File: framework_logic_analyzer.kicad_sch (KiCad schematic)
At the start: 76 parts, among them IC1 TXU0104QWBQARQ1, IC2 TXU0104QWBQARQ1, IC3 TXU0104QWBQARQ1, IC4 TXU0104QWBQARQ1, IC5 CYUSB3014-BZXC, J1 Conn_02x08_Odd_Even, J2 Conn_02x08_Odd_Even, J3 Conn_ARM_JTAG_SWD_10, Q1 MMBT3904, Q2 MMBT3904, Q3 MMBT3904, U5 M24M02-DR, Y1 19.200 MHz

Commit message: New header and enclosure
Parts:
- J1, J2: footprint Connector_PinSocket_1.27mm:PinSocket_2x08_P1.27mm_Horizontal -> 20021311-00016T4LF:20021311-00016T4LF
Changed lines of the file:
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@@
       (effects (font (size 1.27 1.27)))
     )
-    (property "Footprint" "Connector_PinSocket_1.27mm:PinSocket_2x08_P1.27mm_Horizontal" (at 350.52 149.86 0)
+    (property "Footprint" "20021311-00016T4LF:20021311-00016T4LF" (at 350.52 149.86 0)
       (effects (font (size 1.27 1.27)) hide)
     )
@@
       (effects (font (size 1.27 1.27)))
     )
-    (property "Footprint" "Connector_PinSocket_1.27mm:PinSocket_2x08_P1.27mm_Horizontal" (at 350.52 120.65 0)
-      (effects (font (size 1.27 1.27)) hide)
-    )
+    (property "Footprint" "20021311-00016T4LF:20021311-00016T4LF" (at 350.52 120.65 0)
+      (effects (font (size 1.27 1.27)) hide)
+    )

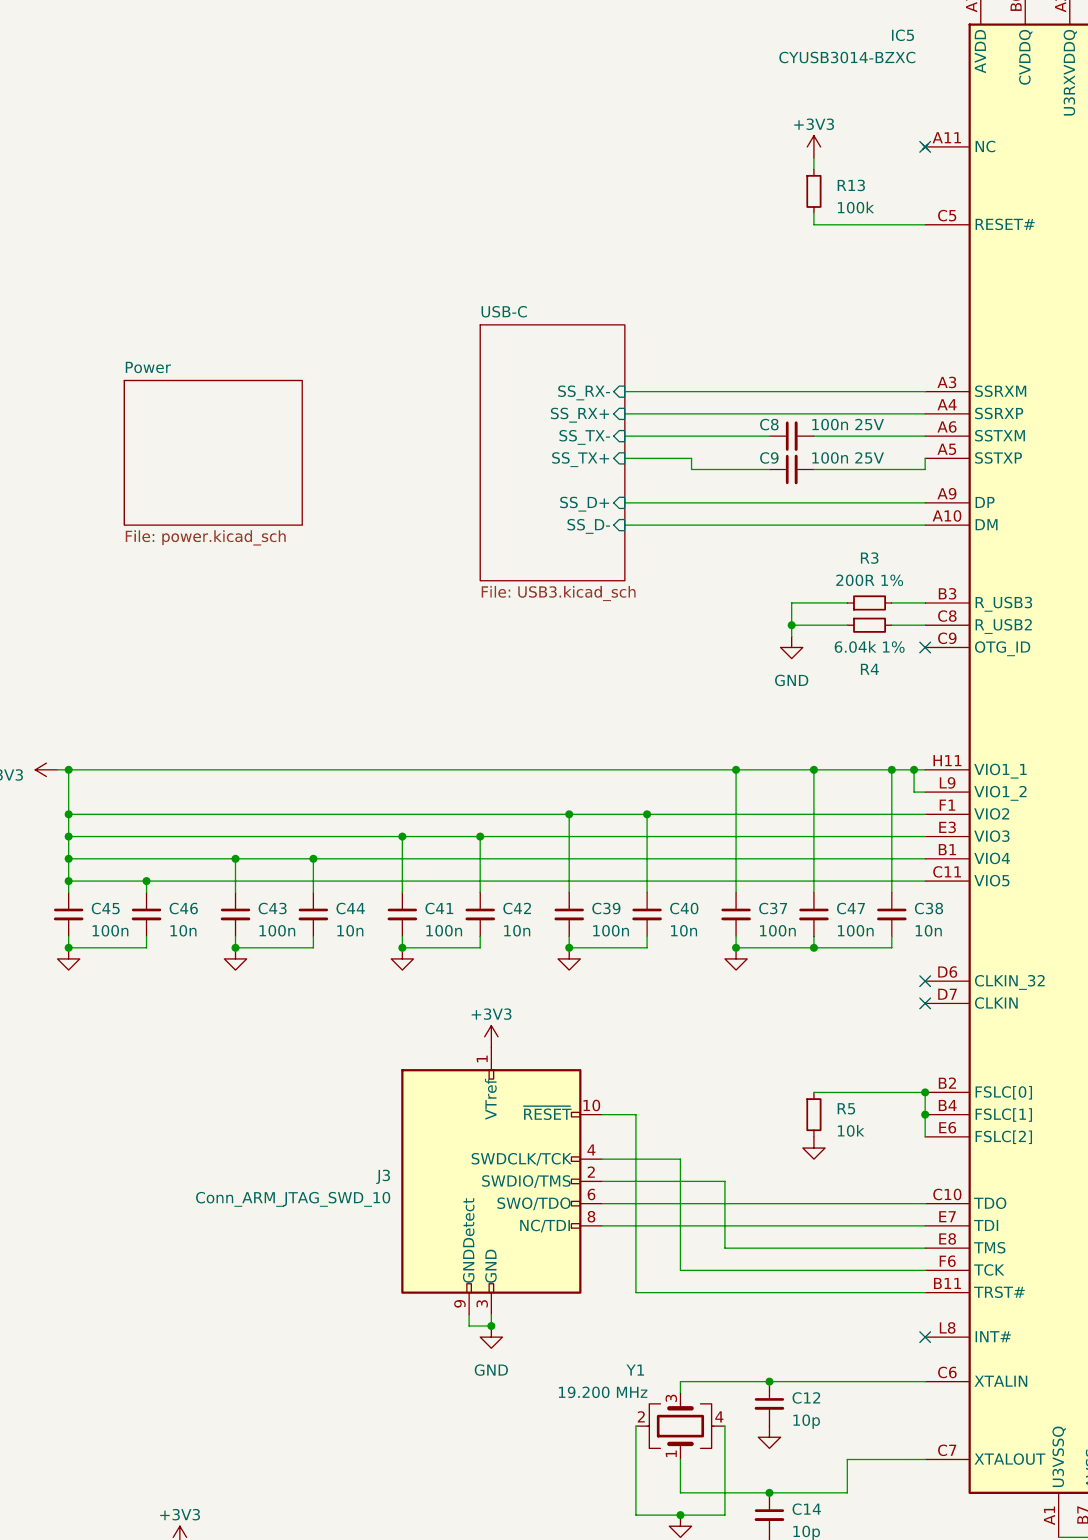
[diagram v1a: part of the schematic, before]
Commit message: Remove jtag header, add reset button
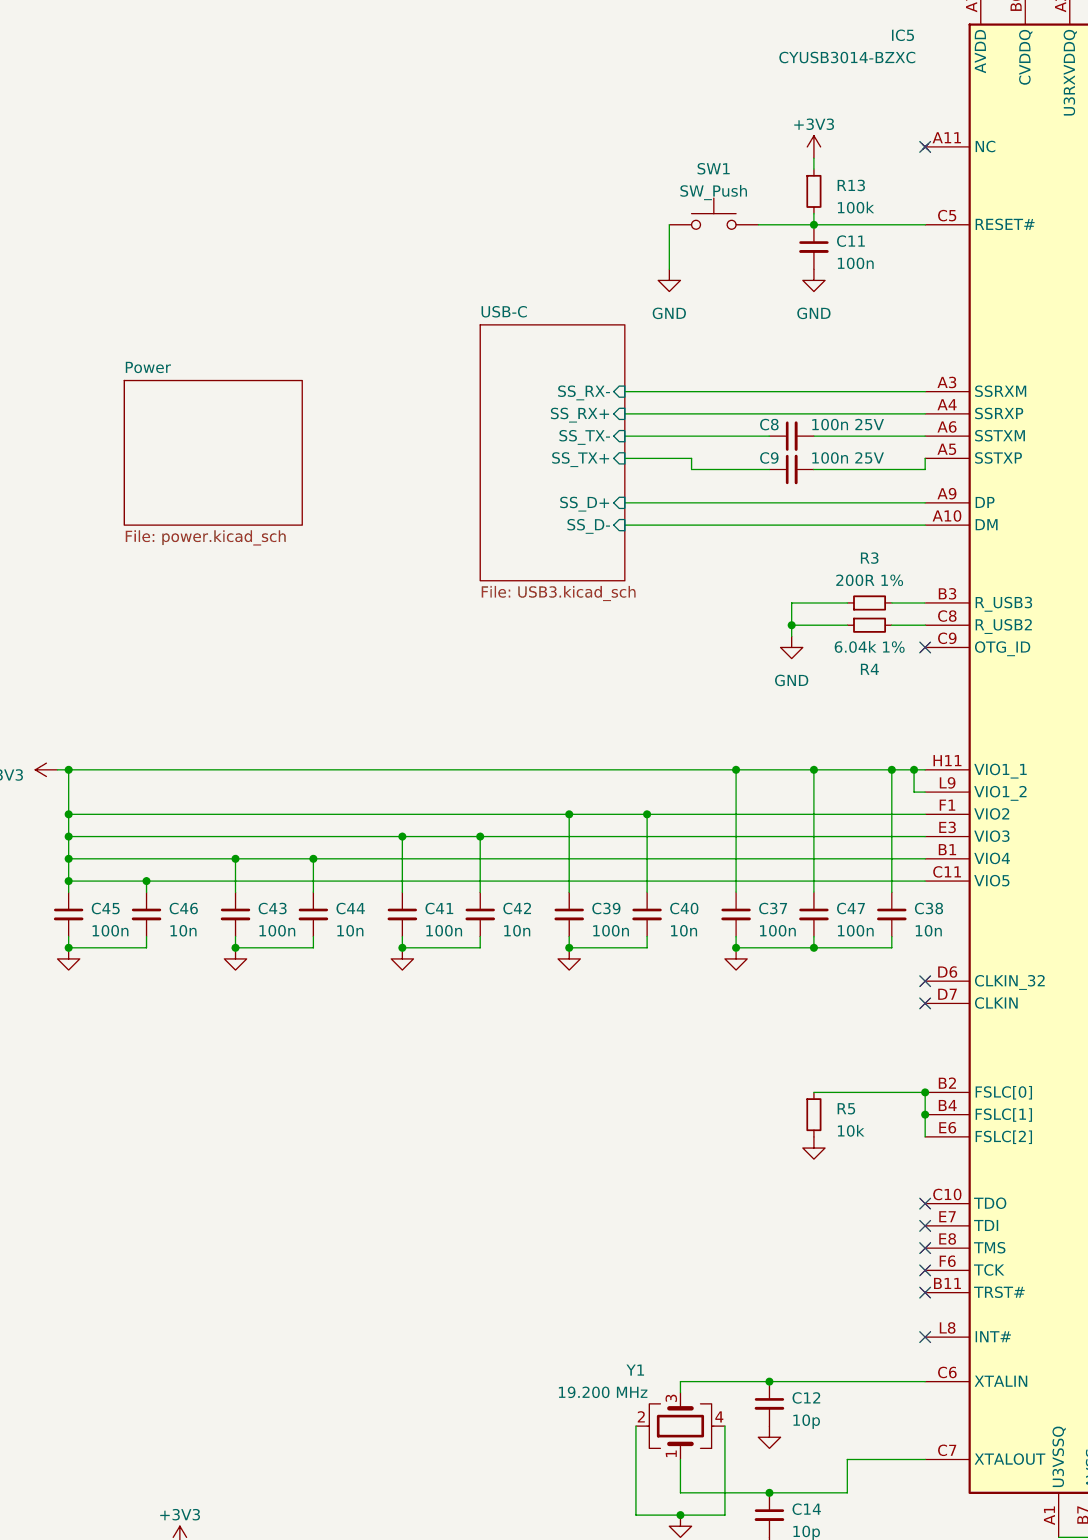
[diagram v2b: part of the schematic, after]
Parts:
- removed J3: Conn_ARM_JTAG_SWD_10, Connector_PinHeader_1.27mm:PinHeader_2x05_P1.27mm_Vertical, symbol Connector:Conn_ARM_JTAG_SWD_10
- added C11: 100n, Capacitor_SMD:C_0402_1005Metric, symbol Device:C_Small
- added SW1: SW_Push, Button_Switch_SMD:SW_Push_SPST_NO_Alps_SKRK, symbol Switch:SW_Push
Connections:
- net GND: now also C11.2, SW1.1
- net at IC5.C5 (RESET#), R13.2: now also C11.1, SW1.2
- no-connect marks 62 -> 67

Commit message: added part nums
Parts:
- IC1, IC2, IC3, IC4: lcsc (none) -> C4354911
- IC5: lcsc (none) -> C462526
- Q1, Q2, Q3: lcsc (none) -> C20526
- SW1: LCSC C262416 -> (none); lcsc (none) -> C262416
- U5: lcsc (none) -> C115042
- Y1: lcsc (none) -> C253771
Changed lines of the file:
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@@
       (effects (font (size 1.27 1.27)) (justify left top) hide)
+    )
+    (property "lcsc" "C4354911" (at 279.4 50.8 0)
+      (effects (font (size 1.27 1.27)) hide)
     )
     (pin "1")
@@
       (effects (font (size 1.27 1.27)) (justify left) hide)
     )
+    (property "lcsc" "C20526" (at 314.96 231.14 0)
+      (effects (font (size 1.27 1.27)) hide)
+    )
     (pin "1")
     (pin "2")
@@
       (effects (font (size 1.27 1.27)) (justify left) hide)
     )
+    (property "lcsc" "C20526" (at 375.92 231.14 0)
+      (effects (font (size 1.27 1.27)) hide)
+    )
     (pin "1")
     (pin "2")
@@
     (property "Arrow Price/Stock" "https://www.arrow.com/en/products/txu0104qwbqarq1/texas-instruments?region=nac" (at 252.73 1201.93 0)
       (effects (font (size 1.27 1.27)) (justify left top) hide)
+    )
+    (property "lcsc" "C4354911" (at 279.4 214.63 0)
+      (effects (font (size 1.27 1.27)) hide)
     )
     (pin "1")
@@
       (effects (font (size 1.27 1.27)) (justify left top) hide)
     )
+    (property "lcsc" "C4354911" (at 279.4 160.02 0)
+      (effects (font (size 1.27 1.27)) hide)
+    )
     (pin "1")
     (pin "10")
@@
       (effects (font (size 1.27 1.27)) hide)
     )
+    (property "lcsc" "C115042" (at 59.69 262.89 0)
+      (effects (font (size 1.27 1.27)) hide)
+    )
     (pin "1")
     (pin "2")
@@
     (property "Arrow Price/Stock" "https://www.arrow.com/en/products/cyusb3014-bzxc/infineon-technologies-ag?region=nac" (at 189.23 1087.63 0)
       (effects (font (size 1.27 1.27)) (justify left top) hide)
+    )
+    (property "lcsc" "C462526" (at 144.78 92.71 0)
+      (effects (font (size 1.27 1.27)) hide)
     )
     (pin "A1")
@@
       (effects (font (size 1.27 1.27)) hide)
     )
-    (property "LCSC" "C262416" (at 120.65 102.87 0)
+    (property "LCSC" "" (at 120.65 102.87 0)
+      (effects (font (size 1.27 1.27)) hide)
+    )
+    (property "lcsc" "C262416" (at 120.65 102.87 0)
       (effects (font (size 1.27 1.27)) hide)
     )
@@
       (effects (font (size 1.27 1.27)) (justify left) hide)
     )
+    (property "lcsc" "C20526" (at 345.44 231.14 0)
+      (effects (font (size 1.27 1.27)) hide)
+    )
     (pin "1")
     (pin "2")
@@
     )
     (property "Datasheet" "~" (at 116.84 240.03 0)
+      (effects (font (size 1.27 1.27)) hide)
+    )
+    (property "lcsc" "C253771" (at 116.84 240.03 90)
       (effects (font (size 1.27 1.27)) hide)
     )
@@
       (effects (font (size 1.27 1.27)) (justify left top) hide)
     )
-    (pin "1")
+    (property "lcsc" "C4354911" (at 279.4 105.41 0)
+      (effects (font (size 1.27 1.27)) hide)
+    )
+    (pin "1")

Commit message: fixed things
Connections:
- net +3V3 renamed +3.3V
- no-connect marks 67 -> 66
